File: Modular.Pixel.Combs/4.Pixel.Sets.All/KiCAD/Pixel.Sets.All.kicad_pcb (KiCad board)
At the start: 2 copper layers, 245 x 78 mm, 58 parts

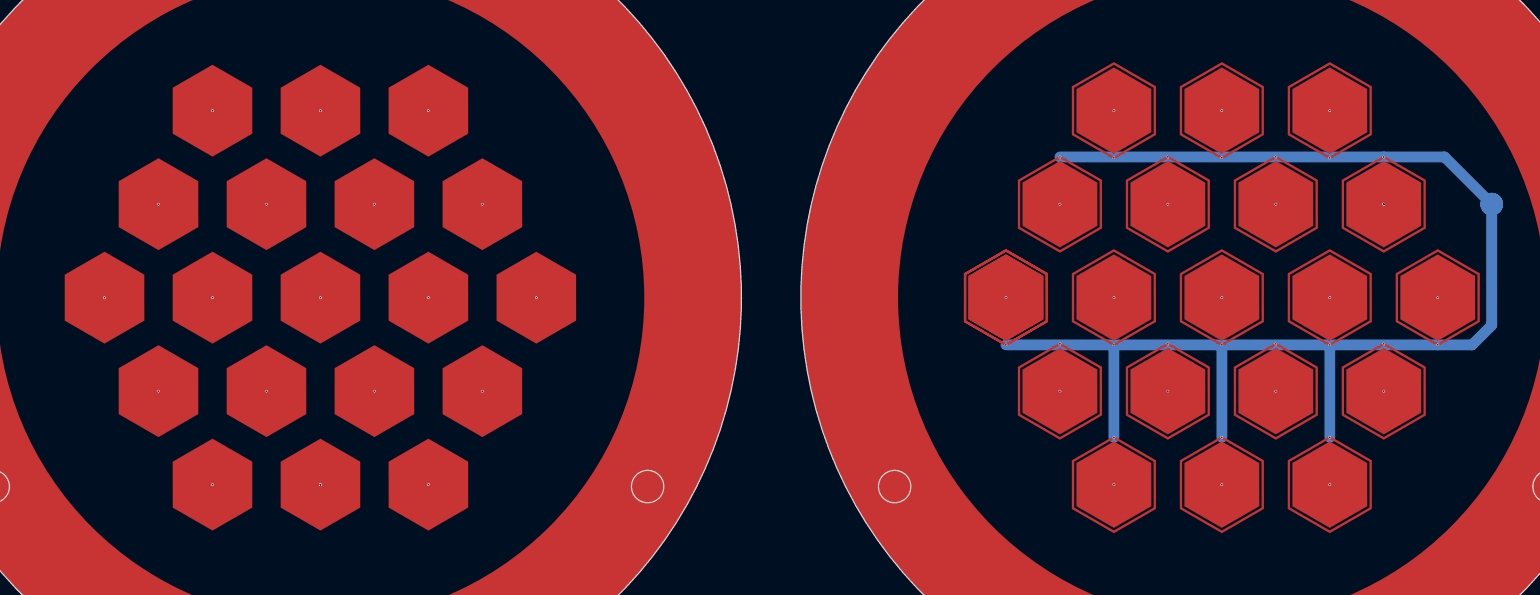
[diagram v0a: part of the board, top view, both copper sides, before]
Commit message: Smoothed out Hexagon Pixels so that it Better Fits the Stencils
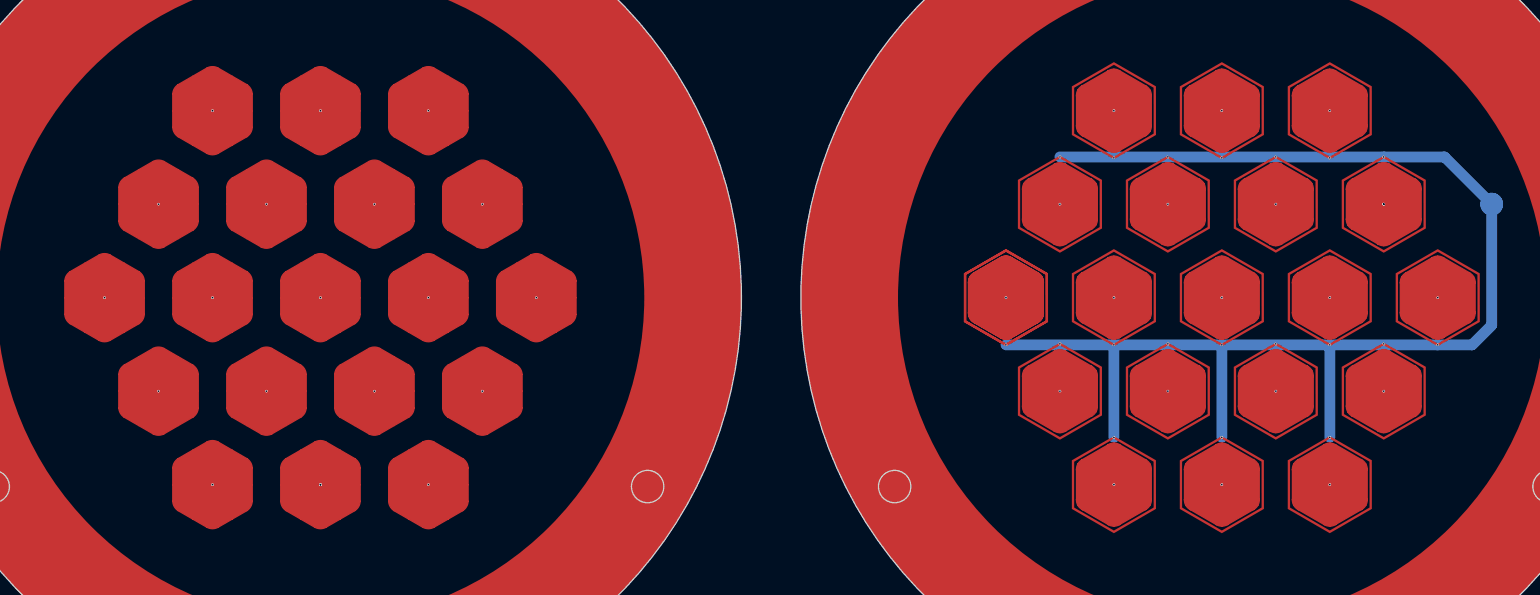
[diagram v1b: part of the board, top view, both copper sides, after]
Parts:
- removed the REF** at (65.0, 58.3)
- removed REF**1, REF**19, REF**2, REF**20, REF**21, REF**23, REF**24, REF**25, REF**31, REF**32, REF**35, REF**36, REF**39, REF**4, REF**40, REF**49, REF**5, REF**8: Hex.Tile.Solid.Hex, Hex:Hex.Tile.Solid.Hex
- added REF**: Hex.Tile.Solid.Hex, 1.Hex:Hex.Tile.Solid.Hex, F.Cu at (65.0, 75.6)
- added REF**: Hex.Tile.Solid.Hex, 1.Hex:Hex.Tile.Solid.Hex, F.Cu at (70.0, 67.0)
- added REF**: Hex.Tile.Solid.Hex, 1.Hex:Hex.Tile.Solid.Hex, F.Cu at (55.0, 75.6)
- added REF**: Hex.Tile.Solid.Hex, 1.Hex:Hex.Tile.Solid.Hex, F.Cu at (60.0, 49.6)
- added REF**: Hex.Tile.Solid.Hex, 1.Hex:Hex.Tile.Solid.Hex, F.Cu at (85.0, 58.3)
- added REF**: Hex.Tile.Solid.Hex, 1.Hex:Hex.Tile.Solid.Hex, F.Cu at (80.0, 67.0)
- added REF**: Hex.Tile.Solid.Hex, 1.Hex:Hex.Tile.Solid.Hex, F.Cu at (55.0, 58.3)
- added REF**: Hex.Tile.Solid.Hex, 1.Hex:Hex.Tile.Solid.Hex, F.Cu at (50.0, 49.6)
- added REF**: Hex.Tile.Solid.Hex, 1.Hex:Hex.Tile.Solid.Hex, F.Cu at (75.0, 58.3)
- added REF**: Hex.Tile.Solid.Hex, 1.Hex:Hex.Tile.Solid.Hex, F.Cu at (65.0, 41.0)
- added REF**: Hex.Tile.Solid.Hex, 1.Hex:Hex.Tile.Solid.Hex, F.Cu at (75.0, 41.0)
- added REF**: Hex.Tile.Solid.Hex, 1.Hex:Hex.Tile.Solid.Hex, F.Cu at (50.0, 67.0)
- added REF**: Hex.Tile.Solid.Hex, 1.Hex:Hex.Tile.Solid.Hex, F.Cu at (60.0, 67.0)
- added REF**: Hex.Tile.Solid.Hex, 1.Hex:Hex.Tile.Solid.Hex, F.Cu at (75.0, 75.6)
- added REF**: Hex.Tile.Solid.Hex, 1.Hex:Hex.Tile.Solid.Hex, F.Cu at (55.0, 41.0)
- added REF**: Hex.Tile.Solid.Hex, 1.Hex:Hex.Tile.Solid.Hex, F.Cu at (80.0, 49.6)
- added REF**: Hex.Tile.Solid.Hex, 1.Hex:Hex.Tile.Solid.Hex, F.Cu at (45.0, 58.3)
- added REF**: Hex.Tile.Solid.Hex, 1.Hex:Hex.Tile.Solid.Hex, F.Cu at (70.0, 49.6)
- added REF**: Hex.Tile.Solid.Hex, 1.Hex:Hex.Tile.Solid.Hex, F.Cu at (65.0, 58.3)
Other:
- board text added: "Pixel Board A ::: May 2023 Alfredo Barajas Enriquez"
- board text added: "Pixel Board B ::: May 2023 Alfredo Barajas Enriquez"
- board text added: "Pixel Board C ::: May 2023 Alfredo Barajas Enriquez"
- board text removed: "Pixel Set A ::: May 2023 Alfredo Barajas Enriquez"
- board text removed: "Pixel Set B ::: May 2023 Alfredo Barajas Enriquez"
- board text removed: "Pixel Set C ::: May 2023 Alfredo Barajas Enriquez"

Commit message: Finalized Pixel Plane Design
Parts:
- removed the REF** at (232.0, 58.3)
- removed REF**10, REF**11, REF**13, REF**14, REF**15, REF**3, REF**30, REF**33, REF**38, REF**50, REF**53, REF**6, REF**64, REF**67, REF**68, REF**71, REF**80, REF**9: Hex.Tile.Solid.G.Dot, Hex:Hex.Tile.Solid.G.Dot
- added REF**: Hex.Tile.Solid.G.Dot, 1.Hex:Hex.Tile.Solid.G.Dot, F.Cu at (222.0, 41.0)
- added REF**: Hex.Tile.Solid.G.Dot, 1.Hex:Hex.Tile.Solid.G.Dot, F.Cu at (242.0, 75.6)
- added REF**: Hex.Tile.Solid.G.Dot, 1.Hex:Hex.Tile.Solid.G.Dot, F.Cu at (247.0, 67.0)
- added REF**: Hex.Tile.Solid.G.Dot, 1.Hex:Hex.Tile.Solid.G.Dot, F.Cu at (217.0, 67.0)
- added REF**: Hex.Tile.Solid.G.Dot, 1.Hex:Hex.Tile.Solid.G.Dot, F.Cu at (252.0, 58.3)
- added REF**: Hex.Tile.Solid.G.Dot, 1.Hex:Hex.Tile.Solid.G.Dot, F.Cu at (247.0, 49.6)
- added REF**: Hex.Tile.Solid.G.Dot, 1.Hex:Hex.Tile.Solid.G.Dot, F.Cu at (242.0, 58.3)
- added REF**: Hex.Tile.Solid.G.Dot, 1.Hex:Hex.Tile.Solid.G.Dot, F.Cu at (217.0, 49.6)
- added REF**: Hex.Tile.Solid.G.Dot, 1.Hex:Hex.Tile.Solid.G.Dot, F.Cu at (212.0, 58.3)
- added REF**: Hex.Tile.Solid.G.Dot, 1.Hex:Hex.Tile.Solid.G.Dot, F.Cu at (237.0, 67.0)
- added REF**: Hex.Tile.Solid.G.Dot, 1.Hex:Hex.Tile.Solid.G.Dot, F.Cu at (242.0, 41.0)
- added REF**: Hex.Tile.Solid.G.Dot, 1.Hex:Hex.Tile.Solid.G.Dot, F.Cu at (227.0, 49.6)
- added REF**: Hex.Tile.Solid.G.Dot, 1.Hex:Hex.Tile.Solid.G.Dot, F.Cu at (232.0, 41.0)
- added REF**: Hex.Tile.Solid.G.Dot, 1.Hex:Hex.Tile.Solid.G.Dot, F.Cu at (232.0, 58.3)
- added REF**: Hex.Tile.Solid.G.Dot, 1.Hex:Hex.Tile.Solid.G.Dot, F.Cu at (222.0, 75.6)
- added REF**: Hex.Tile.Solid.G.Dot, 1.Hex:Hex.Tile.Solid.G.Dot, F.Cu at (222.0, 58.3)
- added REF**: Hex.Tile.Solid.G.Dot, 1.Hex:Hex.Tile.Solid.G.Dot, F.Cu at (232.0, 75.6)
- added REF**: Hex.Tile.Solid.G.Dot, 1.Hex:Hex.Tile.Solid.G.Dot, F.Cu at (237.0, 49.6)
- added REF**: Hex.Tile.Solid.G.Dot, 1.Hex:Hex.Tile.Solid.G.Dot, F.Cu at (227.0, 67.0)

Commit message: Minor Fixes
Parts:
- added G***: LOGO, LOGO, B.Cu at (158.2, 88.2)
- added G***: LOGO, LOGO, B.Cu at (241.7, 88.2)
- added G***: LOGO, LOGO, B.Cu at (74.6, 87.9)
